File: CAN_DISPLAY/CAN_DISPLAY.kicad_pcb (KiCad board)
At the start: 4 copper layers, 188 x 103 mm, 115 parts, among them J1 DISPLAY, J10 DCDC 5V 3A, J11 Micro_SD_Card, J12 J-Link, J13 Prodrammer, J14 Display, J15 LED Display, J2 I2C Sensor 1, J3 I2C Sensor 2, J4 43-01199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

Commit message: PCB Fixes
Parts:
- removed D6: 1N4007, Diode_THT:D_DO-41_SOD81_P10.16mm_Horizontal
- removed J12: J-Link, Connector_JST:JST_PH_B7B-PH-K_1x07_P2.00mm_Vertical
- added D12: 1N5822, Diode_THT:D_DO-201AD_P15.24mm_Horizontal, F.Cu at (86.4, 133.6)
- added G***: LOGO, 1Display:Logo, F.Cu at (216.4, 70.6)
- added J16: BME280 Module, Connector_PinHeader_2.54mm:PinHeader_1x04_P2.54mm_Vertical, F.Cu at (196.9, 144.8)
- added J18: J-Link, Connector_PinHeader_2.54mm:PinHeader_2x10_P2.54mm_Vertical, F.Cu at (194.6, 53.8)
- added JP21: JVDD, Jumper:SolderJumper-2_P1.3mm_Open_RoundedPad1.0x1.5mm, F.Cu at (190.9, 56.9)
- C20: value 10u -> 47u; footprint Capacitor_SMD:CP_Elec_6.3x4.5 -> Capacitor_SMD:CP_Elec_5x5.8
- moved D5 38.4 mm to (190.0, 76.6)
- moved R11 38.4 mm to (190.0, 73.2)
- moved C30 11.0 mm to (193.9, 91.0)
- moved JP12 11.0 mm to (189.3, 88.0)
- moved JP13 11.0 mm to (191.9, 88.0)
- moved JP20 11.0 mm to (194.6, 88.0)
- moved R23 11.0 mm to (189.3, 84.3)
- moved R24 11.0 mm to (191.9, 84.3)
- moved F1 1.53 mm to (74.7, 140.7)
- moved C20 0.78 mm to (142.7, 146.0)
- moved C24 0.66 mm to (146.4, 72.6)
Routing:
- net /ESP32/GPIO_13: track 94.1 -> 72.1 mm, vias 1 -> 2
- net /ESP32/GPIO_12: track 69.7 -> 87.4 mm
- net /ESP32/GPIO_22: track 23.8 -> 35.9 mm
- net +3V3: track 343.6 -> 355.4 mm, vias 5 -> 6
- net /ESP32/GPIO_21: track 18.7 -> 29.7 mm
- net /ESP32/GPIO_14: track 70.2 -> 77.2 mm, vias 0 -> 1
- net I2C_SCL: track 89.9 -> 95.3 mm
- net /ESP32/GPIO_03_U0RXD: track 16.2 -> 20.6 mm
- net Net-(D12-A): track 10.9 -> 15.3 mm
- net Net-(J18-Pin_1): track 0.00 -> 4.31 mm
- net /ESP32/EN: track 135.7 -> 133.0 mm, vias 1 -> 2
- net Net-(D12-K): track 17.0 -> 14.4 mm
- net /ESP32/GPIO_19: track 66.7 -> 69.1 mm
- net /ESP32/GPIO_05: track 94.4 -> 96.4 mm
- net /ESP32/GPIO_26: track 67.0 -> 68.6 mm
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- added copper zone on B.Cu, net GND
- added copper zone on B.Cu, net GND2
- added copper zone on B.Cu, net GND3
- added copper zone on B.Cu, net GNDPWR
- removed copper zone on In1.Cu, net GND2
- removed copper zone on In1.Cu, net GND3
- removed copper zone on In1.Cu, net GNDPWR

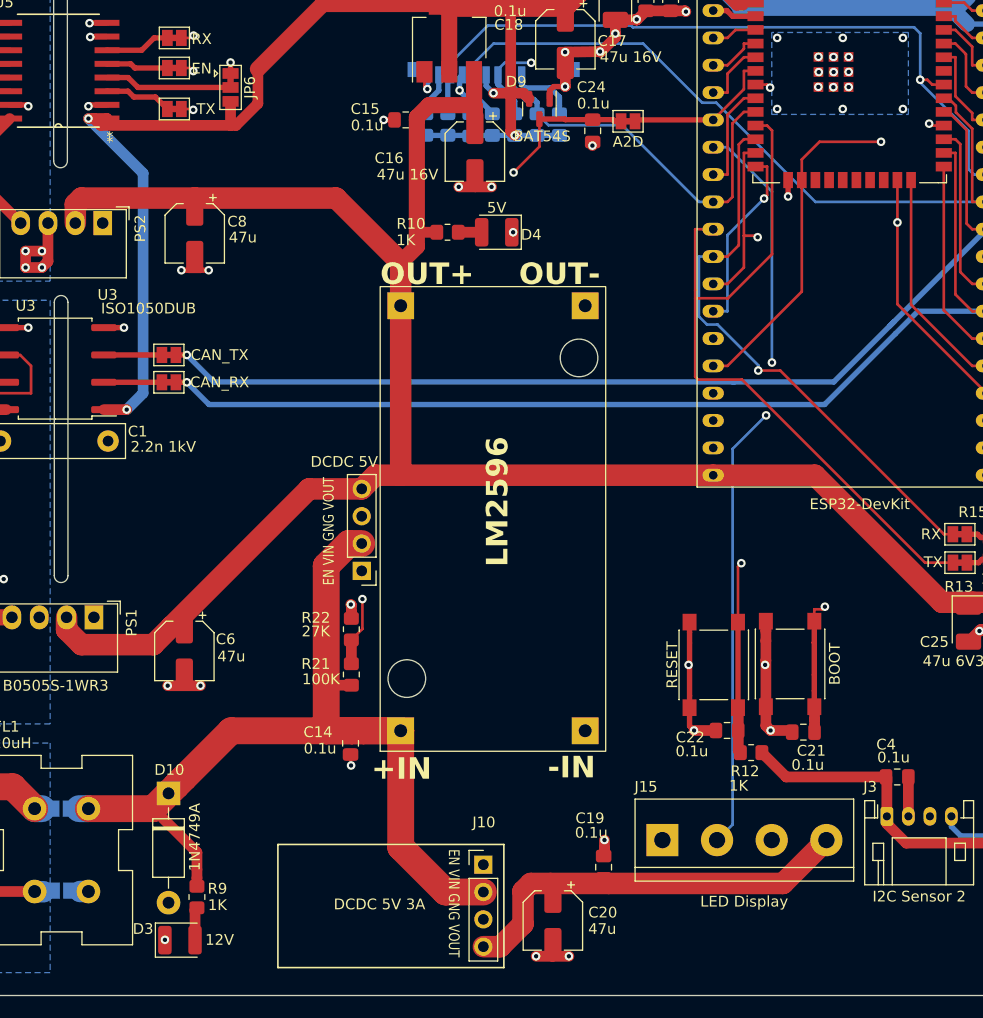
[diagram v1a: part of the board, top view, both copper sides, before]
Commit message: Add Ambient Light
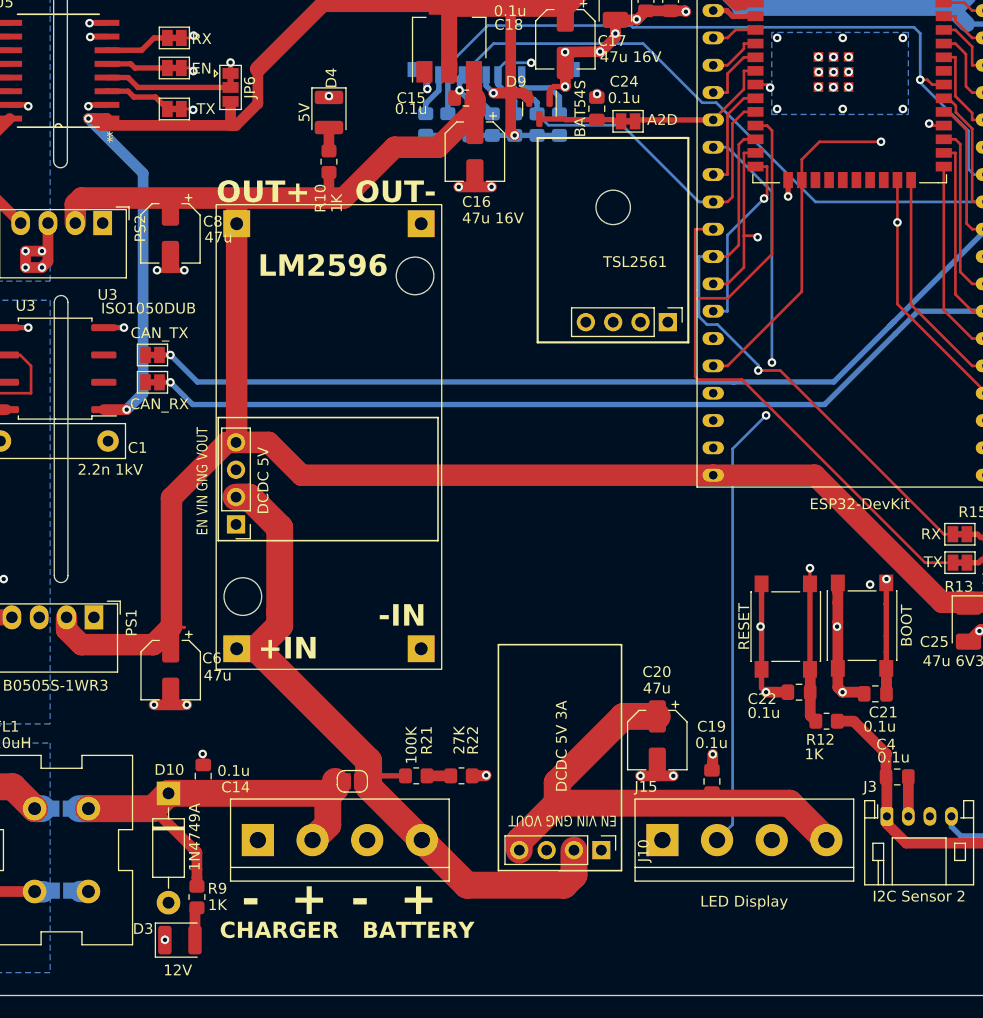
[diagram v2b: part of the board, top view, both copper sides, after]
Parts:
- added J17: CHARGER, TerminalBlock:TerminalBlock_bornier-4_P5.08mm, F.Cu at (115.3, 138.6)
- added J19: TSL2561, Connector_PinHeader_2.54mm:PinHeader_1x04_P2.54mm_Vertical, F.Cu at (153.4, 90.4)
- added JP23: Open, Jumper:SolderJumper-2_P1.3mm_Open_RoundedPad1.0x1.5mm, F.Cu at (124.1, 133.1)
- moved C20 19.4 mm to (152.4, 129.3)
- moved D4 19.2 mm to (121.9, 70.9), turned to -90 degrees
- moved R22 17.0 mm to (134.2, 132.6), turned to 180 degrees
- moved PS3 17.0 mm to (113.3, 120.8)
- moved C14 14.0 mm to (110.2, 132.6), turned to 90 degrees
- moved C19 12.8 mm to (157.5, 133.1)
- moved R10 12.8 mm to (121.9, 75.5), turned to -90 degrees
- moved J8 12.5 mm to (113.3, 109.2)
- moved R21 11.2 mm to (130.0, 132.6), turned to 180 degrees
- moved J10 11.0 mm to (147.2, 139.5), turned to -90 degrees
- moved R12 7.59 mm to (168.2, 127.5)
- moved C21 7.58 mm to (172.7, 125.0)
- moved C22 7.58 mm to (165.6, 124.8)
- moved SW2 7.58 mm to (164.4, 118.7)
- moved SW1 7.58 mm to (171.5, 118.6)
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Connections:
- C14 pad 1: +12V -> /PowerSuply/12V_FL
- D10 pad 1: +12V -> /PowerSuply/12V_FL
- FL1 pad 2: +12V -> /PowerSuply/12V_FL
- JP16 pad 1: +12V -> /PowerSuply/12V_FL
- R9 pad 2: +12V -> /PowerSuply/12V_FL
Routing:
- net A2D_12V: track 65.8 -> 10.1 mm, vias 2 -> 0
- net /PowerSuply/12V_FL: track 0.00 -> 41.7 mm
- net +12V: track 97.5 -> 64.0 mm
- net +5VP: track 38.4 -> 46.7 mm
- net /ESP32/GPIO_00_BOOT: track 69.5 -> 62.9 mm
- net CANBUS_TO_TX: track 5.40 -> 0.00 mm
- net CANBUS_TO_RX: track 5.40 -> 0.00 mm
- net +3V3: track 355.4 -> 350.9 mm
- net /ESP32/GPIO_05: track 96.4 -> 97.9 mm
- net /ESP32/GPIO_04: track 97.5 -> 99.1 mm
- net +5V: track 207.0 -> 206.3 mm
- net /ESP32/EN: track 133.0 -> 132.4 mm
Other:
- outline, holes or cut-outs redrawn
- board text added: "CHARGER BATTERY"

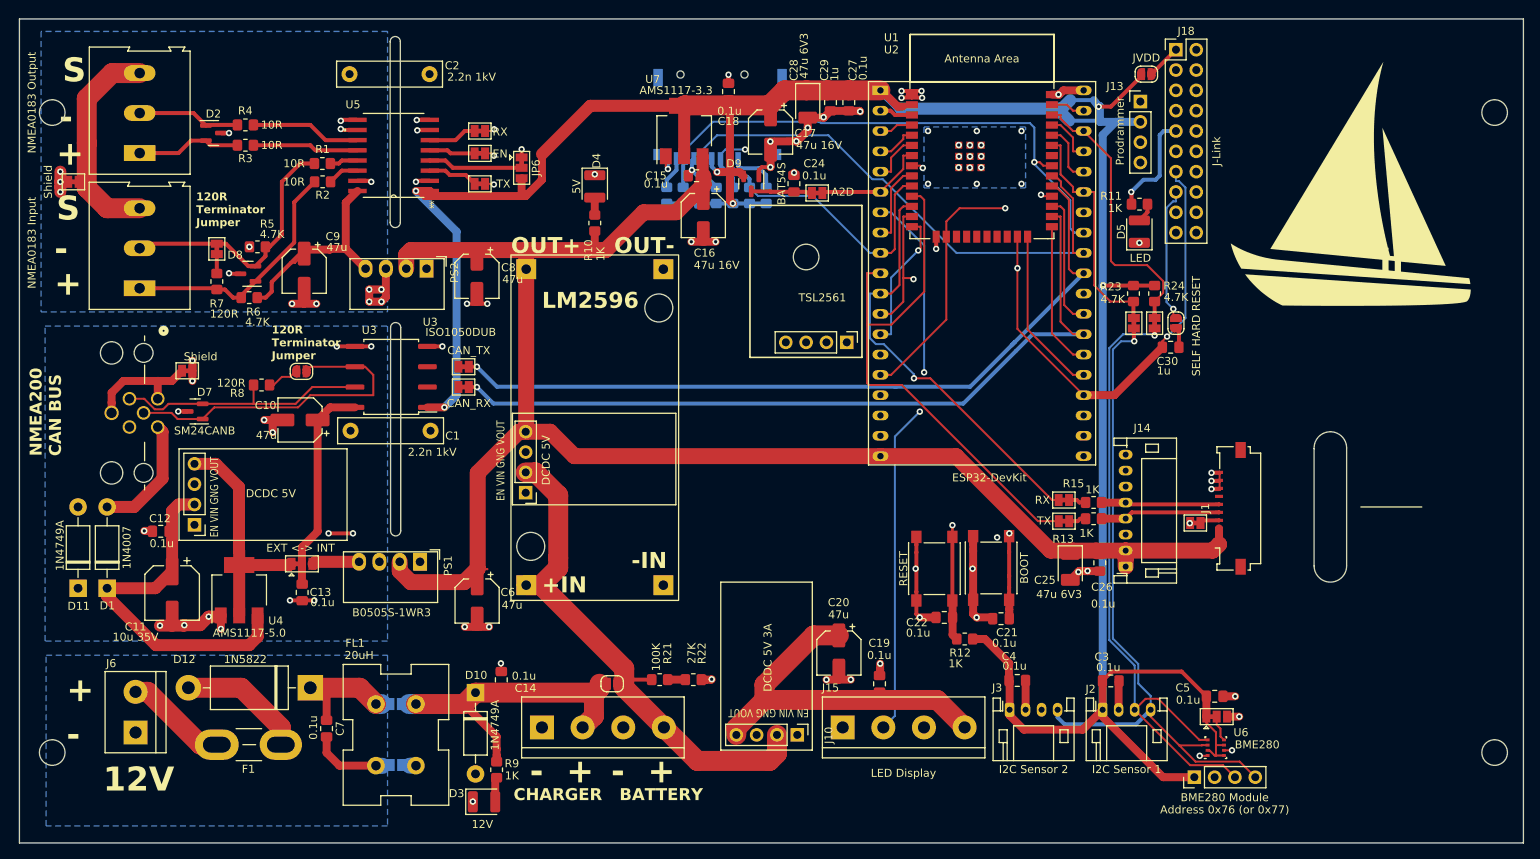
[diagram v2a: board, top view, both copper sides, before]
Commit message: Added Light Sensor
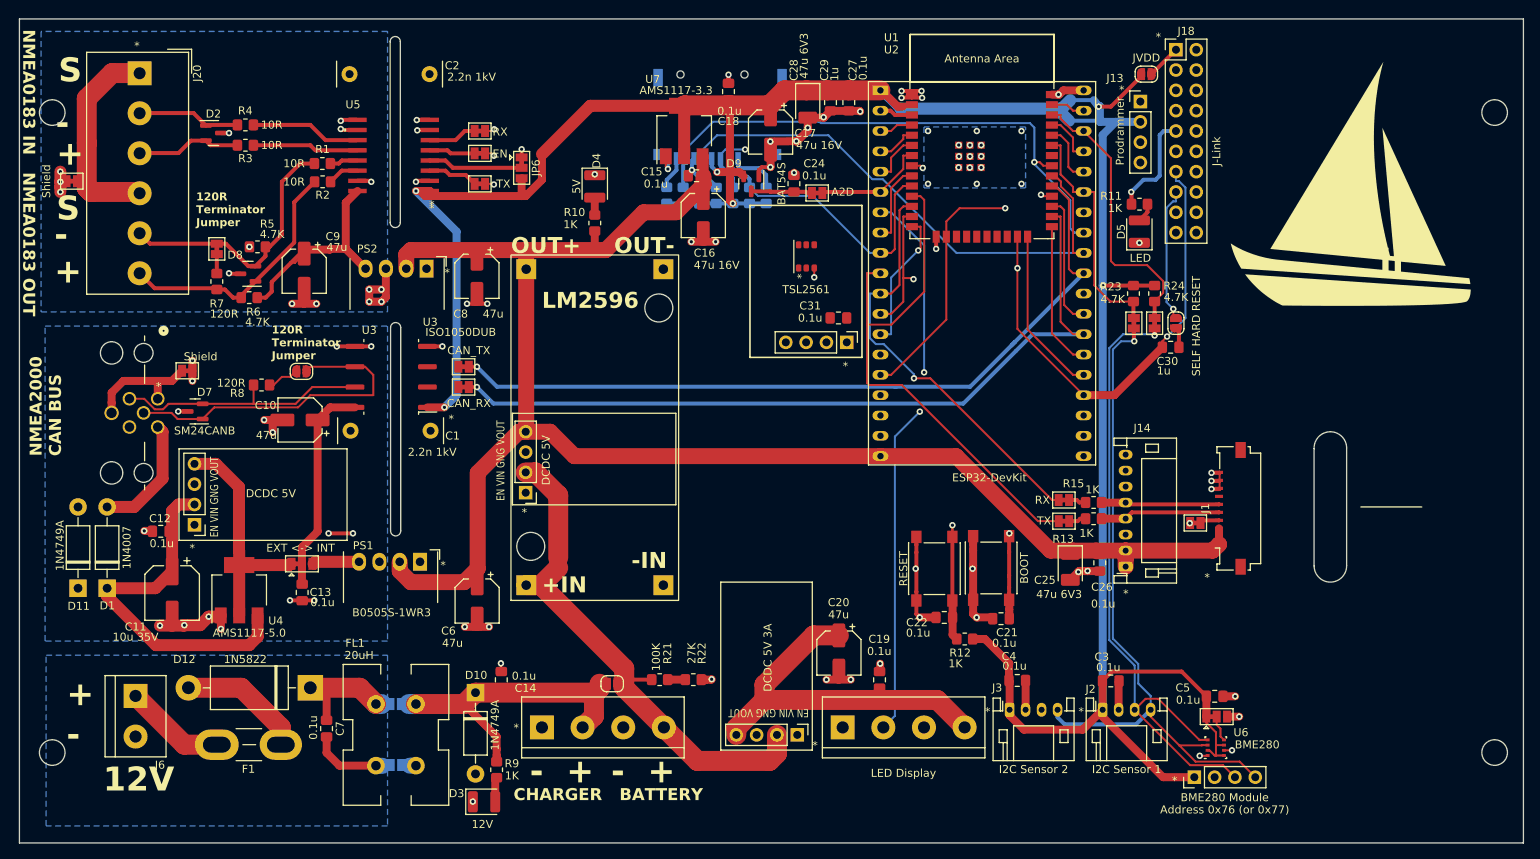
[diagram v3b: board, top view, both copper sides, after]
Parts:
- removed J5: NMEA0183 Output, TerminalBlock:TerminalBlock_Altech_AK300-3_P5.00mm
- removed J7: NMEA0183 Input, TerminalBlock:TerminalBlock_Altech_AK300-3_P5.00mm
- added C31: 0.1u, Capacitor_SMD:C_0805_2012Metric_Pad1.18x1.45mm_HandSolder, F.Cu at (152.4, 87.4)
- added J20: NMEA0183, TerminalBlock_Altech:Altech_AK300_1x06_P5.00mm_45-Degree, F.Cu at (65.0, 56.8)
- added LED1: TSL2561, 1Display:TSL2561, F.Cu at (146.8, 81.7)
- moved J6 4.57 mm to (64.5, 134.6), turned to -90 degrees
- moved C19 0.50 mm to (157.5, 132.6)
- moved JP5 0.22 mm to (56.5, 70.3)
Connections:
- F1 pad 1: Net-(J6-Pin_2) -> Net-(J6-Pin_1)
- J6 pad 1: GNDPWR -> Net-(J6-Pin_1)
- J6 pad 2: Net-(J6-Pin_2) -> GNDPWR
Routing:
- net Net-(J6-Pin_2): track 12.9 -> 0.00 mm
- net Net-(J6-Pin_1): track 0.00 -> 12.7 mm
- net +12V: track 64.0 -> 62.7 mm
- net +5V: track 206.3 -> 205.0 mm
- net Net-(J20-Pin_1): track 32.0 -> 31.2 mm
- net /Isolated/NMEA OUT+: track 31.5 -> 32.2 mm
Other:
- outline, holes or cut-outs redrawn
- board text added: "*"
- board text added: "NMEA0183 IN NMEA0183 OUT"
- board text added: "NMEA2000 CAN BUS"
- board text removed: "NMEA200 CAN BUS"

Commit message: Add SW
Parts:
- removed J17: CHARGER, TerminalBlock:TerminalBlock_bornier-4_P5.08mm
- added BZ1: Buzzer, Buzzer_Beeper:Buzzer_12x9.5RM7.6, F.Cu at (148.3, 101.4)
- added D6: 1N4007, Diode_THT:D_DO-41_SOD81_P10.16mm_Horizontal, F.Cu at (139.7, 100.6)
- added J5: Power, TerminalBlock:TerminalBlock_bornier-5_P5.08mm, F.Cu at (114.0, 139.4)
- added JP24: BUZZER, Jumper:SolderJumper-2_P1.3mm_Bridged_Pad1.0x1.5mm, F.Cu at (157.5, 114.3)
- added JP25: Open, Jumper:SolderJumper-2_P1.3mm_Open_RoundedPad1.0x1.5mm, F.Cu at (124.3, 133.1)
- added Q1: BC547, Package_TO_SOT_SMD:SOT-23, F.Cu at (149.3, 114.2)
- added R25: 1K, Resistor_SMD:R_0805_2012Metric_Pad1.20x1.40mm_HandSolder, F.Cu at (153.9, 114.3)
- D3, D4, D5: footprint LED_SMD:LED_1210_3225Metric -> LED_SMD:LED_0805_2012Metric_Pad1.15x1.40mm_HandSolder
- J4: value 43-01199 -> NMEA2000
- moved JP23 3.59 mm to (120.5, 133.1)
- moved J18 2.03 mm to (196.6, 53.8)
- moved JP21 1.19 mm to (192.0, 56.6), turned to 90 degrees
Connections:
- JP23 pad 1: +12V -> Net-(J5-Pin_4)
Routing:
- net A2D_12V: track 10.1 -> 75.0 mm, vias 0 -> 2
- net I2C_SDA: track 86.8 -> 147.4 mm
- net I2C_SCL: track 95.3 -> 154.0 mm
- net +3V3: track 350.9 -> 376.8 mm
- net GND: track 130.6 -> 149.3 mm, vias 65 -> 91
- net Net-(BZ1-+): track 0.00 -> 13.7 mm
- net /ESP32/GPIO_14: track 77.2 -> 64.6 mm, vias 1 -> 2
- net +5V: track 205.0 -> 217.3 mm
- net /ESP32/GPIO_12: track 87.4 -> 75.8 mm, vias 1 -> 2
- net Net-(J5-Pin_4): track 0.00 -> 11.2 mm
- net /ESP32/GPIO_13: track 72.1 -> 62.2 mm
- net /ESP32/EN: track 132.4 -> 122.5 mm, vias 2 -> 3
- net Net-(Q1-B): track 0.00 -> 4.95 mm
- net CANBUS_TO_TX: track 0.00 -> 3.87 mm
- net CANBUS_TO_RX: track 0.00 -> 3.87 mm
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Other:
- outline, holes or cut-outs redrawn
- board text added: "+12V"
- board text added: "+5V"
- board text added: "CHARGER BATTERY SW"
- board text added: "Direct +12V"
- board text removed: "CHARGER BATTERY"

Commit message: Release Version 1.00 Rev 1.00
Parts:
- added C32: 0.1u, Capacitor_SMD:C_0805_2012Metric_Pad1.18x1.45mm_HandSolder, F.Cu at (85.6, 74.4)
- added C33: 0.1u, Capacitor_SMD:C_0805_2012Metric_Pad1.18x1.45mm_HandSolder, F.Cu at (104.6, 77.2)
- moved G*** 3.41 mm to (219.5, 69.1)
- moved R7 1.79 mm to (74.7, 81.0)
- moved JP18 1.38 mm to (74.7, 77.4)
- moved R5 1.27 mm to (79.8, 77.2)
- moved C19 1.17 mm to (157.5, 131.4)
- moved D8 1.10 mm to (78.7, 80.8)
- moved R6 1.02 mm to (78.7, 83.8)
- moved C11 0.89 mm to (69.3, 120.9)
- moved C9 0.76 mm to (85.6, 80.8)
- moved D12 0.25 mm to (86.6, 133.6)
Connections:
- JP24 pad 1: /ESP32/GPIO_33_32K -> /ESP32/GPIO_14
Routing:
- net /ESP32/GPIO_14: track 64.6 -> 93.2 mm, vias 2 -> 3
- net GND: track 149.3 -> 174.7 mm, vias 91 -> 96
- net GND2: track 30.4 -> 23.7 mm, vias 16 -> 13
- net +3V3: track 376.8 -> 371.9 mm
- net /ESP32/GPIO_32_32K: track 79.1 -> 83.4 mm
- net /ESP32/GPIO_17: track 93.1 -> 95.8 mm
- net /PowerSuply/12V_FL: track 40.8 -> 38.1 mm
- net /ESP32/GPIO_22: track 35.9 -> 34.0 mm
- net +5VP: track 46.7 -> 48.4 mm
- net Net-(D1-A): track 15.5 -> 16.9 mm
- net GND3: track 26.4 -> 27.8 mm, vias 15 -> 16
- net /ESP32/GPIO_33_32K: track 76.4 -> 75.3 mm, vias 1 -> 0
- net +5V: track 217.3 -> 218.3 mm
- net /Isolated/NMEA OUT+: track 33.3 -> 32.3 mm
- net Net-(D1-K): track 50.2 -> 51.1 mm
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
